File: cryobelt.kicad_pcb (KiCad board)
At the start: 4 copper layers, 90 x 50 mm, 92 parts, among them J1 Speaker, J2 Charge, J3 Battery, J4 Fan, Q1 AO3401A, Q2 AO3400A, Q3 AO3401A, Q4 AO3400A, SW1 Reset, SW2 Boot, SW3 Down, SW4 User, SW5 Up, U1 SHT4x, U2 ESP32-S3-MINI-1, U3 MAX98357A, U4 FUSB303BTMX, U5 TPS61089, U6 D3V3XA4B10LP, U7 BQ25895RTW, U8 TPS63001, U9 INA180A3

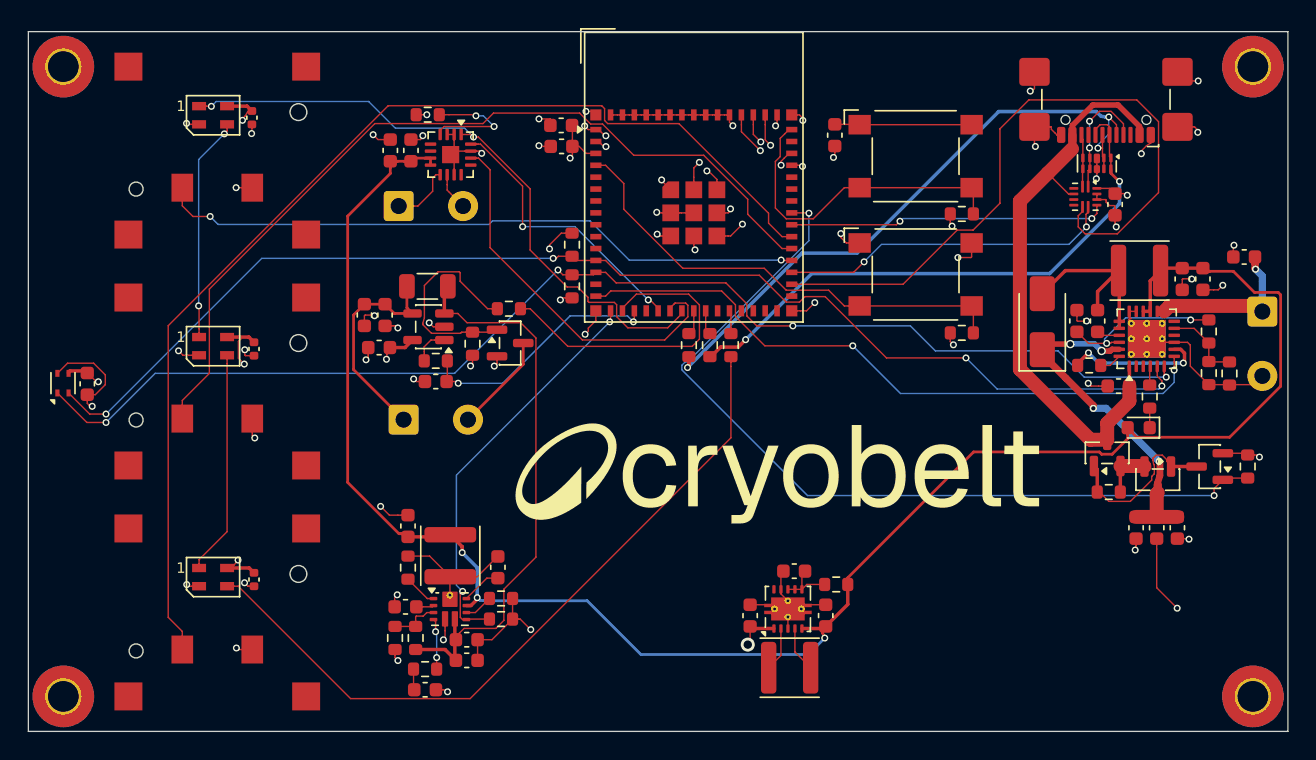
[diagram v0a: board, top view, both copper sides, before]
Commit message: Fixed DOUT short circuit
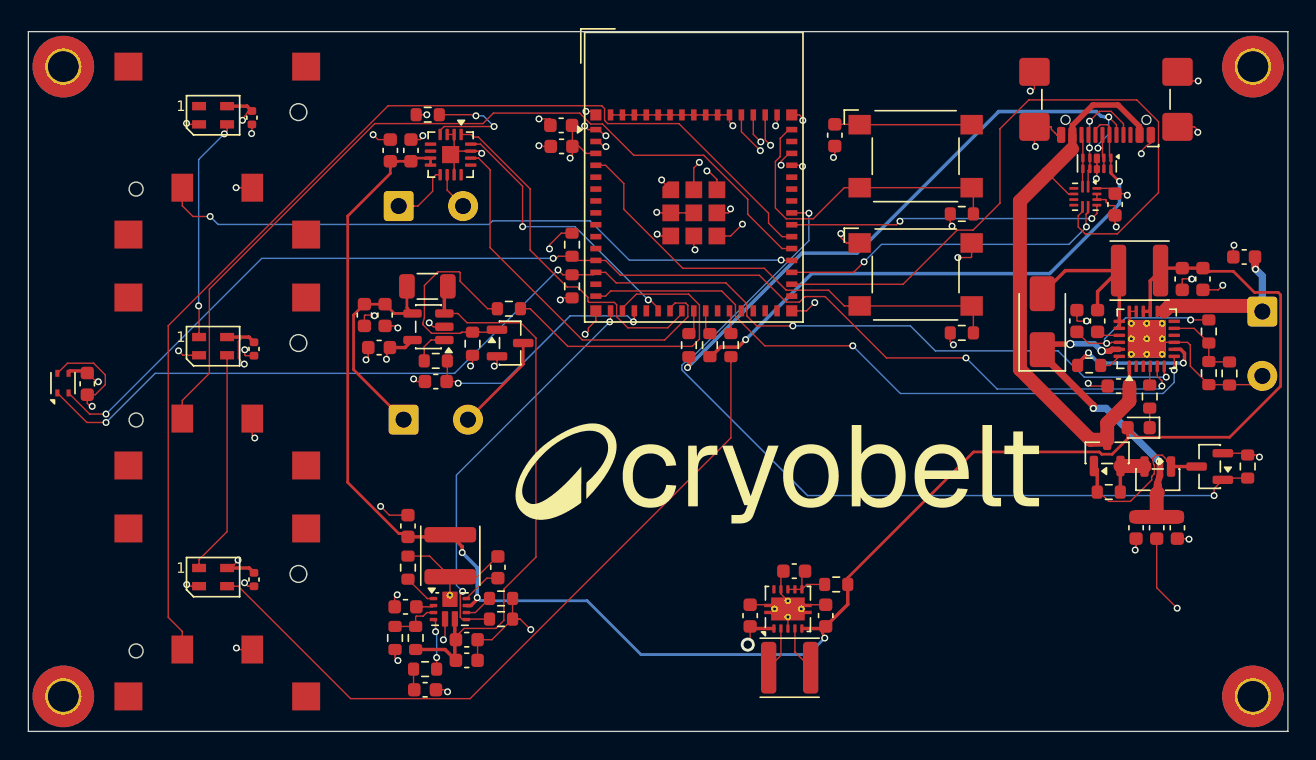
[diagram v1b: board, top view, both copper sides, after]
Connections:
- D3 pad 1: /ESP32-S3/DOUT -> unconnected-(D3-DOUT-Pad1)
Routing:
- net /ESP32-S3/DOUT: track 46.2 -> 25.1 mm, vias 2 -> 0
- net GND: track 148.0 -> 141.1 mm
- net VDC: track 134.2 -> 132.2 mm
- net +3V3: track 41.3 -> 39.3 mm
- net /Power/PMID: track 24.9 -> 23.6 mm
- net +12V: track 40.7 -> 40.0 mm
- net /ESP32-S3/D+: track 41.2 -> 40.6 mm
- net +BATT: track 12.0 -> 11.4 mm
- net Net-(J1-Pin_2): track 2.71 -> 2.17 mm

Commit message: BQ fixes
i hate my life
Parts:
- added R26: 100R, Resistor_SMD:R_0603_1608Metric, F.Cu at (188.5, 101.7)
- added TP1: TestPoint, TestPoint:TestPoint_Pad_D2.0mm, F.Cu at (192.4, 84.5)
- added TP2: TestPoint, TestPoint:TestPoint_Pad_D2.0mm, F.Cu at (145.4, 107.5)
- added TP3: TestPoint, TestPoint:TestPoint_Pad_D2.0mm, F.Cu at (152.8, 117.0)
- added TP4: TestPoint, TestPoint:TestPoint_Pad_D2.0mm, F.Cu at (192.3, 88.3)
- renumbered C14 to C12, C12 to C13, C13 to C14, R14 to R11, R15 to R12, R16 to R13, R17 to R14, R18 to R15, R19 to R16, R20 to R17, R21 to R18, R22 to R19, R23 to R20, R24 to R21, R25 to R22, R26 to R23, R27 to R24, R28 to R25
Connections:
- U7 pad 10: unconnected-(U7-ILIM-Pad10) -> Net-(U7-ILIM)
- U8 pad 10: unconnected-(U8-FB-Pad10) -> +3V3
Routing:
- net VBUS: track 42.9 -> 61.7 mm
- net +3V3: track 39.3 -> 48.3 mm
- net Net-(U7-ILIM): track 0.00 -> 6.56 mm, vias 0 -> 2
- net +12V: track 40.0 -> 45.5 mm
- net +BATT: track 11.4 -> 14.3 mm
- net GND: track 141.1 -> 142.6 mm

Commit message: Fix more bugs
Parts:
- added C28: 10uF, Capacitor_SMD:C_0603_1608Metric, F.Cu at (155.1, 116.7)
- added R17: 10k, Resistor_SMD:R_0603_1608Metric, F.Cu at (170.9, 102.7)
- added R18: 100k, Resistor_SMD:R_0603_1608Metric, F.Cu at (188.1, 85.0)
- moved TP2 5.48 mm to (143.5, 112.7)
- moved TP3 2.60 mm to (150.2, 117.0)
- renumbered C28 to C29, C29 to C30, C30 to C31, C31 to C32, C32 to C33, R26 to R19, R17 to R20, R18 to R21, R19 to R22, R20 to R23, R21 to R24, R22 to R25, R23 to R26, R24 to R27, R25 to R28
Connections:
- C1 pad 1: Net-(C1-Pad1) -> /ESP32-S3/EN
- SW1 pad 1: Net-(C1-Pad1) -> GND
- U2 pad 41: unconnected-(U2-IO45-Pad41) -> /ESP32-S3/OTG
- U7 pad 8: +3V3 -> /ESP32-S3/OTG
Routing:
- net /ESP32-S3/OTG: track 0.00 -> 45.0 mm, vias 0 -> 3
- net GND: track 142.6 -> 157.7 mm
- net Net-(C1-Pad1): track 9.75 -> 0.00 mm
- net /ESP32-S3/~{BQ_INT}: track 47.2 -> 51.0 mm, vias 2 -> 3
- net +3V3: track 48.3 -> 51.9 mm, vias 15 -> 16
- net /ESP32-S3/EN: track 23.1 -> 26.3 mm
- net +12V: track 45.5 -> 42.3 mm

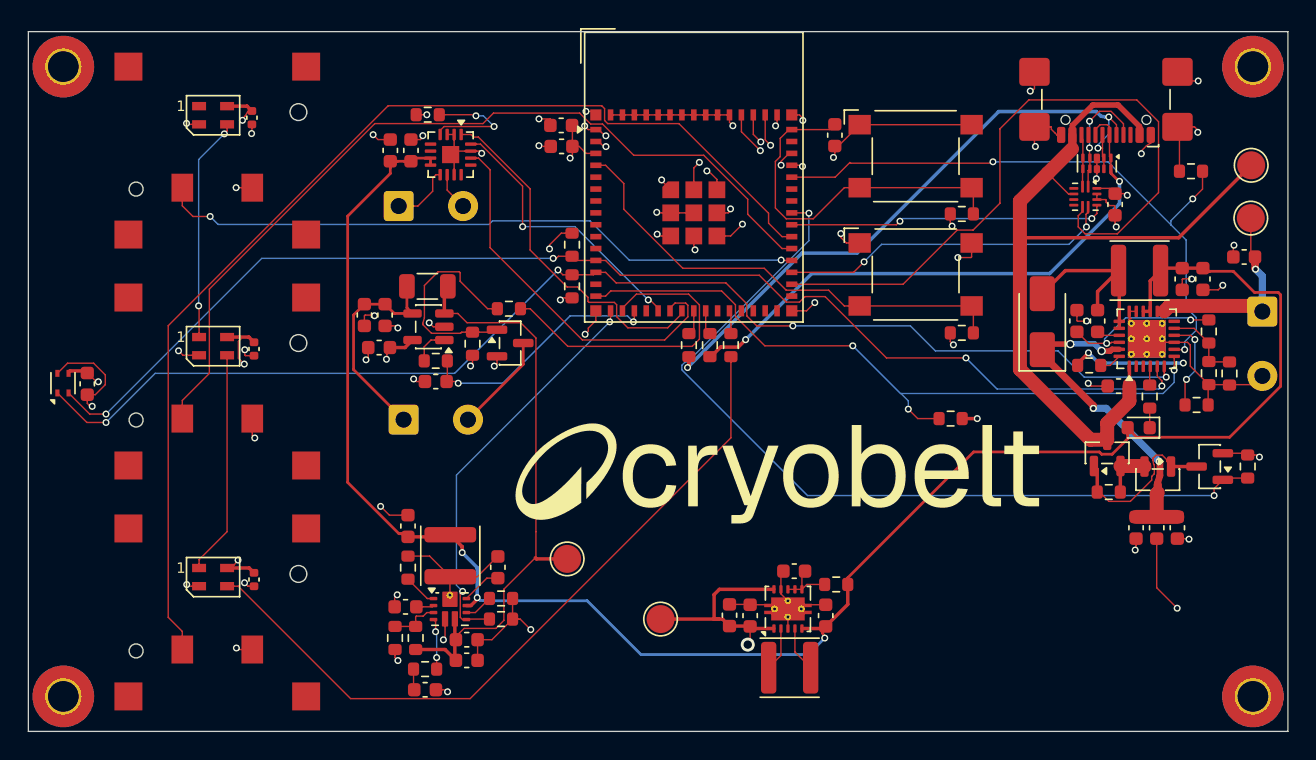
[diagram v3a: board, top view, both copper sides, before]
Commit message: Finalize routed Cryobelt PCB for fabrication
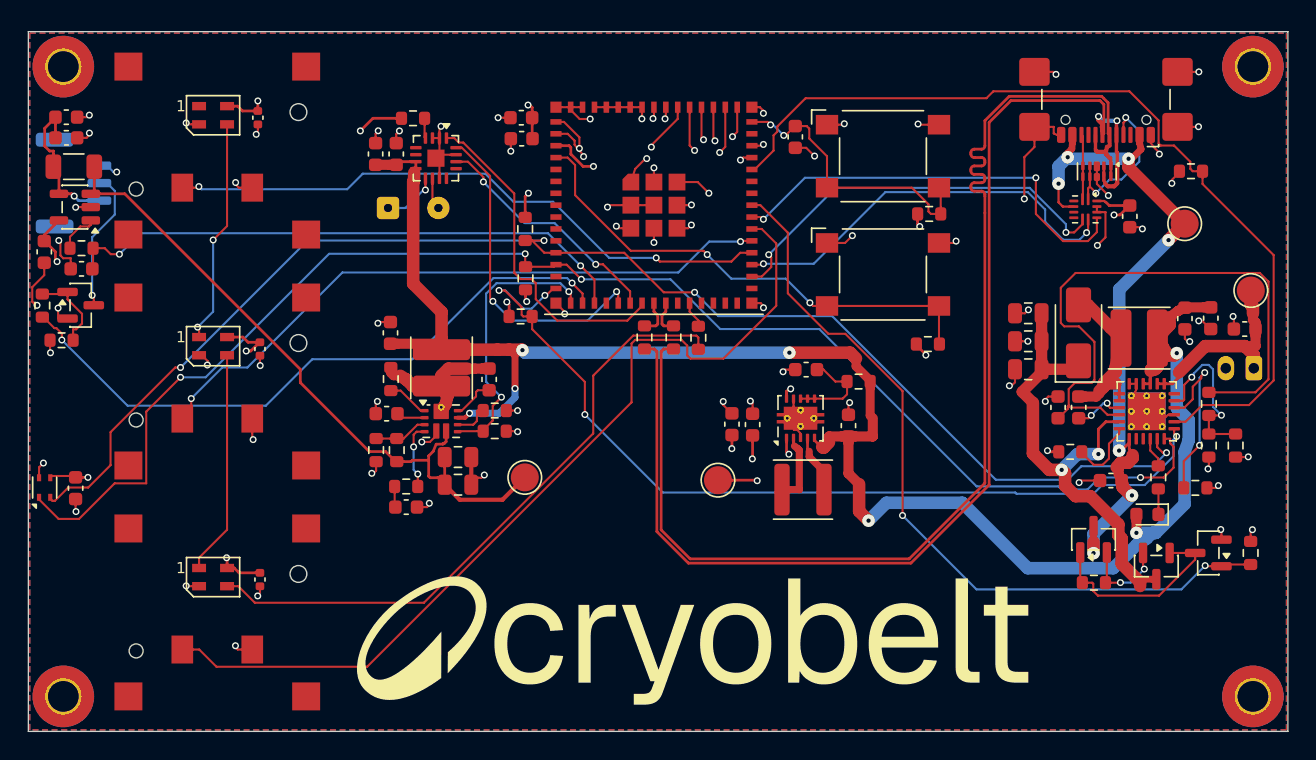
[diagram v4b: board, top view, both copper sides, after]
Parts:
- C10, C11, C13, C17, C18: footprint Capacitor_SMD:C_0603_1608Metric -> Capacitor_SMD:C_0805_2012Metric
- J1: footprint Connector_Wire:SolderWire-0.5sqmm_1x02_P4.6mm_D0.9mm_OD2.1mm -> Connector_Wire:SolderWire-0.1sqmm_1x02_P3.6mm_D0.4mm_OD1mm
- J3: footprint Connector_Wire:SolderWire-0.5sqmm_1x02_P4.6mm_D0.9mm_OD2.1mm -> Connector_JST:JST_PH_S2B-PH-K_1x02_P2.00mm_Horizontal; moved to B.Cu
- J4: value Fan -> Conn_01x03_Pin; footprint Connector_Wire:SolderWire-0.5sqmm_1x02_P4.6mm_D0.9mm_OD2.1mm -> Connector_JST:JST_GH_SM03B-GHS-TB_1x03-1MP_P1.25mm_Horizontal; moved to B.Cu
- L1: value 1.8uH -> 2.2uH; footprint Inductor_SMD:L_APV_ANR4020 -> Cryobelt:FEXU0420
- L3: footprint Inductor_SMD:L_APV_ANR4020 -> Cryobelt:FEXU0420
- Q4: value AO3400A -> 2N7002
- R27: value 100R -> 1k
- SW3, SW4, SW5: footprint PG1316:PG1316S -> Cryobelt:PG1316S
- U2: footprint RF_Module:ESP32-S2-MINI-1 -> Cryobelt:ESP32-S3-MINI-1
- U7: footprint Package_DFN_QFN:Texas_RTW_WQFN-24-1EP_4x4mm_P0.5mm_EP2.7x2.7mm_ThermalVias -> Cryobelt:Texas_RTW_WQFN-24-1EP_4x4mm_P0.5mm_EP2.7x2.7mm_ThermalVias
- moved R27 33.3 mm to (106.0, 94.6), turned to -90 degrees
- moved R17 31.6 mm to (140.2, 95.3), turned to 0 degrees
- moved Q4 30.8 mm to (108.7, 94.5)
- moved R28 29.4 mm to (107.4, 97.0), turned to 0 degrees
- moved J4 29.0 mm to (108.2, 85.8), turned to 90 degrees
- moved C32 26.8 mm to (107.7, 81.1), turned to 0 degrees
- moved U9 26.7 mm to (108.3, 87.5)
- moved R25 26.7 mm to (108.2, 84.7)
- moved R26 26.6 mm to (108.8, 90.5)
- moved C31 26.6 mm to (108.8, 92.0)
- moved C30 24.9 mm to (106.1, 90.7), turned to -90 degrees
- moved C33 24.8 mm to (107.7, 82.6), turned to 0 degrees
- moved C13 17.2 mm to (176.4, 95.1), turned to 180 degrees
- moved C11 16.2 mm to (176.4, 97.1), turned to 180 degrees
- moved C10 15.5 mm to (176.4, 99.1), turned to 180 degrees
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- renumbered R7 to R5, R5 to R6, R6 to R7
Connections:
- net /Fan Control/FAN+ renamed +12V_FAN
- net /Fan Control/FAN- renamed Net-(J4-Pin_2)
- net Net-(U2-USB_D+) renamed /ESP32-S3/USB_PHY_D+
- net Net-(U2-USB_D-) renamed /ESP32-S3/USB_PHY_D-
- net Net-(U5-SW) renamed /Power/12V_SW
- R27 pad 1: /ESP32-S3/FAN_GATE -> Net-(Q4-G)
- R27 pad 2: Net-(Q4-G) -> /ESP32-S3/FAN_PWM
- U2 pad 17: /ESP32-S3/FAN_GATE -> /ESP32-S3/FAN_PWM
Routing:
- net /ESP32-S3/D+: track 40.6 -> 87.4 mm, vias 2 -> 0
- net /ESP32-S3/FAN_PWM: track 0.00 -> 46.3 mm, vias 0 -> 2
- net /ESP32-S3/D-: track 45.5 -> 87.5 mm, vias 3 -> 2
- net Net-(U7-REGN): track 11.9 -> 43.7 mm, vias 2 -> 0
- net /ESP32-S3/I_FAN: track 17.8 -> 41.1 mm
- net /ESP32-S3/FAN_GATE: track 22.8 -> 0.00 mm
- net /ESP32-S3/OUT1: track 48.9 -> 28.9 mm, vias 0 -> 2
- net /ESP32-S3/OTG: track 45.0 -> 64.2 mm, vias 3 -> 0
- net Net-(U2-IO39): track 61.5 -> 46.2 mm, vias 0 -> 2
- net Net-(U2-IO40): track 79.4 -> 64.2 mm
- net /ESP32-S3/SDA: track 89.3 -> 103.3 mm
- net /ESP32-S3/~{BQ_INT}: track 51.0 -> 64.7 mm, vias 3 -> 4
- net GND: track 157.7 -> 144.7 mm, vias 69 -> 88
- net VBUS: track 61.7 -> 49.0 mm, vias 0 -> 7
- net /ESP32-S3/SCL: track 88.9 -> 100.9 mm
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- added copper zone on B.Cu, net GND
- added copper zone on F.Cu, net GND

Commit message: Resolve R15 and R25 assembly sourcing
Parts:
- R25: value 0.05R/0.1% -> 0.05R/1%
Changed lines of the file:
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@@
 			)
 		)
-		(property "Manufacturer" "YAGEO"
+		(property "Manufacturer" "PANASONIC"
 			(at 0 0 90)
 			(unlocked yes)
@@
 			)
 		)
-		(property "MPN" "RC0603FR-07953KL"
+		(property "MPN" "ERJ3EKF9533V"
 			(at 0 0 90)
 			(unlocked yes)
@@
 			)
 		)
-		(property "LCSC Part #" "C137669"
+		(property "LCSC Part #" "C403405"
 			(at 0 0 90)
 			(unlocked yes)
@@
 			)
 		)
-		(property "Value" "0.05R/0.1%"
+		(property "Value" "0.05R/1%"
 			(at 0 1.83 0)
 			(layer "F.Fab")

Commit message: Replace SK6805 LEDs with 3.3V WS2812B
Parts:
- D1, D2, D3: value SK6805 -> WS2812B-2427-V6; footprint LED_SMD:LED_SK6805_PLCC4_2.4x2.7mm_P1.3mm -> Cryobelt:WS2812B-2427-V6_Rotated180
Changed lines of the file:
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@@
 		)
 	)
-	(footprint "LED_SMD:LED_SK6805_PLCC4_2.4x2.7mm_P1.3mm"
+	(footprint "Cryobelt:WS2812B-2427-V6_Rotated180"
 		(layer "F.Cu")
 		(at 118.2 113.975)
-		(descr "https://cdn-shop.adafruit.com/product-files/3484/3484_Datasheet.pdf")
-		(tags "LED RGB NeoPixel Nano PLCC-4")
+		(descr "Worldsemi WS2812B-2427-V6; 3.3 V compatible; remapped for 180 degree physical substitution")
+		(tags "LED RGB NeoPixel 2427 3.3V rotated 180")
 		(property "Reference" "D1"
 			(at 0 -2.2 0)
@@
 			)
 		)
-		(property "Value" "SK6805"
+		(property "Value" "WS2812B-2427-V6"
 			(at 0 2.7 0)
 			(layer "F.Fab")
@@
 			)
 		)
-		(property "Datasheet" "https://cdn-shop.adafruit.com/product-files/3484/3484_Datasheet.pdf"
+		(property "Datasheet" "https://atta.szlcsc.com/upload/public/pdf/source/20251224/E1A9CA691775549EA7D4A013FE234DF1.pdf"
 			(at 0 0 0)
 			(unlocked yes)
@@
 			)
 		)
-		(property "Description" "RGB LED with integrated controller"
+		(property "Description" "3.3 V compatible addressable RGB LED; 24-bit 800 kbit/s; footprint remapped for 180 degree substitution"
 			(at 0 0 0)
 			(unlocked yes)
@@
 			)
 		)
-		(property "Manufacturer" "OPSCO Optoelectronics"
+		(property "Manufacturer" "Worldsemi"
 			(at 0 0 0)
 			(unlocked yes)
@@
 			)
 		)
-		(property "MPN" "SK6805MICRO-J"
+		(property "MPN" "WS2812B-2427-V6"
 			(at 0 0 0)
 			(unlocked yes)
@@
 			)
 		)
-		(property "LCSC Part #" "C2909056"
+		(property "LCSC Part #" "C52941389"
 			(at 0 0 0)
 			(unlocked yes)
@@
 			)
 		)
-		(property ki_fp_filters "LED*SK6805*PLCC*2.4x2.7mm*P1.3mm*")
+		(property ki_fp_filters "*WS2812B*2427*Rotated180*")
 		(sheetname "/ESP32-S3/")
 		(sheetfile "ESP32-S3.kicad_sch")
@@
 		)
 		(fp_text user "1"
-			(at -2.3 -0.65 0)
+			(at 2.3 0.65 0)
 			(unlocked yes)
 			(layer "F.SilkS")
@@
 			)
 			(rotate
-				(xyz 0 0 0)
-			)
-		)
-		(model "C:/Users/ASUS/Documents/GitHub/libs/3dmodels/SK6805-2.4x2.7.step"
-			(offset
-				(xyz 0 0 0)
-			)
-			(scale
-				(xyz 1 1 1)
-			)
-			(rotate
-				(xyz 0 0 0)
+				(xyz 0 0 180)
 			)
 		)
@@
 		(embedded_fonts no)
 	)
-	(footprint "LED_SMD:LED_SK6805_PLCC4_2.4x2.7mm_P1.3mm"
+	(footprint "Cryobelt:WS2812B-2427-V6_Rotated180"
 		(layer "F.Cu")
 		(at 118.2 80.975)
-		(descr "https://cdn-shop.adafruit.com/product-files/3484/3484_Datasheet.pdf")
-		(tags "LED RGB NeoPixel Nano PLCC-4")
+		(descr "Worldsemi WS2812B-2427-V6; 3.3 V compatible; remapped for 180 degree physical substitution")
+		(tags "LED RGB NeoPixel 2427 3.3V rotated 180")
 		(property "Reference" "D3"
 			(at 0 -2.2 0)
@@
 			)
 		)
-		(property "Value" "SK6805"
+		(property "Value" "WS2812B-2427-V6"
 			(at 0 2.7 0)
 			(layer "F.Fab")
@@
 			)
 		)
-		(property "Datasheet" "https://cdn-shop.adafruit.com/product-files/3484/3484_Datasheet.pdf"
+		(property "Datasheet" "https://atta.szlcsc.com/upload/public/pdf/source/20251224/E1A9CA691775549EA7D4A013FE234DF1.pdf"
 			(at 0 0 0)
 			(unlocked yes)
@@
 			)
 		)
-		(property "Description" "RGB LED with integrated controller"
+		(property "Description" "3.3 V compatible addressable RGB LED; 24-bit 800 kbit/s; footprint remapped for 180 degree substitution"
 			(at 0 0 0)
 			(unlocked yes)
@@
 			)
 		)
-		(property "Manufacturer" "OPSCO Optoelectronics"
+		(property "Manufacturer" "Worldsemi"
 			(at 0 0 0)
 			(unlocked yes)
@@
 			)
 		)
-		(property "MPN" "SK6805MICRO-J"
+		(property "MPN" "WS2812B-2427-V6"
 			(at 0 0 0)
 			(unlocked yes)
@@
 			)
 		)
-		(property "LCSC Part #" "C2909056"
+		(property "LCSC Part #" "C52941389"
 			(at 0 0 0)
 			(unlocked yes)
@@
 			)
 		)
-		(property ki_fp_filters "LED*SK6805*PLCC*2.4x2.7mm*P1.3mm*")
+		(property ki_fp_filters "*WS2812B*2427*Rotated180*")
 		(sheetname "/ESP32-S3/")
 		(sheetfile "ESP32-S3.kicad_sch")
@@
 		)
 		(fp_text user "1"
-			(at -2.3 -0.65 0)
+			(at 2.3 0.65 0)
 			(unlocked yes)
 			(layer "F.SilkS")
@@
 			)
 			(rotate
-				(xyz 0 0 0)
-			)
-		)
-		(model "C:/Users/ASUS/Documents/GitHub/libs/3dmodels/SK6805-2.4x2.7.step"
-			(offset
-				(xyz 0 0 0)
-			)
-			(scale
-				(xyz 1 1 1)
-			)
-			(rotate
-				(xyz 0 0 0)
+				(xyz 0 0 180)
 			)
 		)
@@
 		)
 	)
-	(footprint "LED_SMD:LED_SK6805_PLCC4_2.4x2.7mm_P1.3mm"
+	(footprint "Cryobelt:WS2812B-2427-V6_Rotated180"
 		(layer "F.Cu")
 		(at 118.2 97.475)
-		(descr "https://cdn-shop.adafruit.com/product-files/3484/3484_Datasheet.pdf")
-		(tags "LED RGB NeoPixel Nano PLCC-4")
+		(descr "Worldsemi WS2812B-2427-V6; 3.3 V compatible; remapped for 180 degree physical substitution")
+		(tags "LED RGB NeoPixel 2427 3.3V rotated 180")
 		(property "Reference" "D2"
 			(at 0 -2.2 0)
@@
 			)
 		)
-		(property "Value" "SK6805"
+		(property "Value" "WS2812B-2427-V6"
 			(at 0 2.7 0)
 			(layer "F.Fab")
@@
 			)
 		)
-		(property "Datasheet" "https://cdn-shop.adafruit.com/product-files/3484/3484_Datasheet.pdf"
+		(property "Datasheet" "https://atta.szlcsc.com/upload/public/pdf/source/20251224/E1A9CA691775549EA7D4A013FE234DF1.pdf"
 			(at 0 0 0)
 			(unlocked yes)
@@
 			)
 		)
-		(property "Description" "RGB LED with integrated controller"
+		(property "Description" "3.3 V compatible addressable RGB LED; 24-bit 800 kbit/s; footprint remapped for 180 degree substitution"
 			(at 0 0 0)
 			(unlocked yes)
@@
 			)
 		)
-		(property "Manufacturer" "OPSCO Optoelectronics"
+		(property "Manufacturer" "Worldsemi"
 			(at 0 0 0)
 			(unlocked yes)
@@
 			)
 		)
-		(property "MPN" "SK6805MICRO-J"
+		(property "MPN" "WS2812B-2427-V6"
 			(at 0 0 0)
 			(unlocked yes)
@@
 			)
 		)
-		(property "LCSC Part #" "C2909056"
+		(property "LCSC Part #" "C52941389"
 			(at 0 0 0)
 			(unlocked yes)
@@
 			)
 		)
-		(property ki_fp_filters "LED*SK6805*PLCC*2.4x2.7mm*P1.3mm*")
+		(property ki_fp_filters "*WS2812B*2427*Rotated180*")
 		(sheetname "/ESP32-S3/")
 		(sheetfile "ESP32-S3.kicad_sch")
@@
 		)
 		(fp_text user "1"
-			(at -2.3 -0.65 0)
+			(at 2.3 0.65 0)
 			(unlocked yes)
 			(layer "F.SilkS")
@@
 			)
 			(rotate
-				(xyz 0 0 0)
-			)
-		)
-		(model "C:/Users/ASUS/Documents/GitHub/libs/3dmodels/SK6805-2.4x2.7.step"
-			(offset
-				(xyz 0 0 0)
-			)
-			(scale
-				(xyz 1 1 1)
-			)
-			(rotate
-				(xyz 0 0 0)
+				(xyz 0 0 180)
 			)
 		)
